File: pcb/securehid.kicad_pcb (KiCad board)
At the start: 2 copper layers, 129 x 69 mm, 193 parts, among them J1 USB_B_Micro, J2 SWD_HOST, J3 UART_HOST, J4 SWD_DEVICE, J5 UART_DEVICE, J6 USB_A, J7 USB_SPARE, J8 USB_A, Q1 AO3400, Q2 AO3400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

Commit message: Some cleanups
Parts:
- removed the REF** at (65.2, 63.0)
- removed the REF** at (65.2, 99.0)
- added REF**: MountingHole_2.7mm_M2.5, MountingHole:MountingHole_2.7mm_M2.5, F.Cu at (96.5, 108.5)
- added REF**: MountingHole_2.7mm_M2.5, MountingHole:MountingHole_2.7mm_M2.5, F.Cu at (146.5, 108.5)
- added REF**: MountingHole_2.7mm_M2.5, MountingHole:MountingHole_2.7mm_M2.5, F.Cu at (146.5, 53.5)
- added REF**: MountingHole_2.7mm_M2.5, MountingHole:MountingHole_2.7mm_M2.5, F.Cu at (96.5, 53.5)
- added REF**: MountingHole_2.7mm_M2.5, MountingHole:MountingHole_2.7mm_M2.5, F.Cu at (51.5, 53.5)
- added REF**: MountingHole_2.7mm_M2.5, MountingHole:MountingHole_2.7mm_M2.5, F.Cu at (51.5, 108.5)
- added TP81: TestPoint_Alt, TestPoint:TestPoint_Pad_1.0x1.0mm, B.Cu at (115.0, 82.2)
- added TP82: TestPoint_Alt, TestPoint:TestPoint_Pad_1.0x1.0mm, B.Cu at (115.0, 85.8)
- added TP83: TestPoint_Alt, TestPoint:TestPoint_Pad_1.0x1.0mm, B.Cu at (115.0, 84.0)
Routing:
- net GND: track 91.3 -> 98.1 mm, vias 9 -> 39
- net /SECURE_IF_F4RX: track 49.8 -> 51.8 mm, vias 0 -> 1
- net /SECURE_IF_F4TX: track 51.1 -> 52.8 mm, vias 0 -> 1
- net GNDA: vias 2 -> 38
- net (no net): vias 0 -> 1
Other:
- outline, holes or cut-outs redrawn

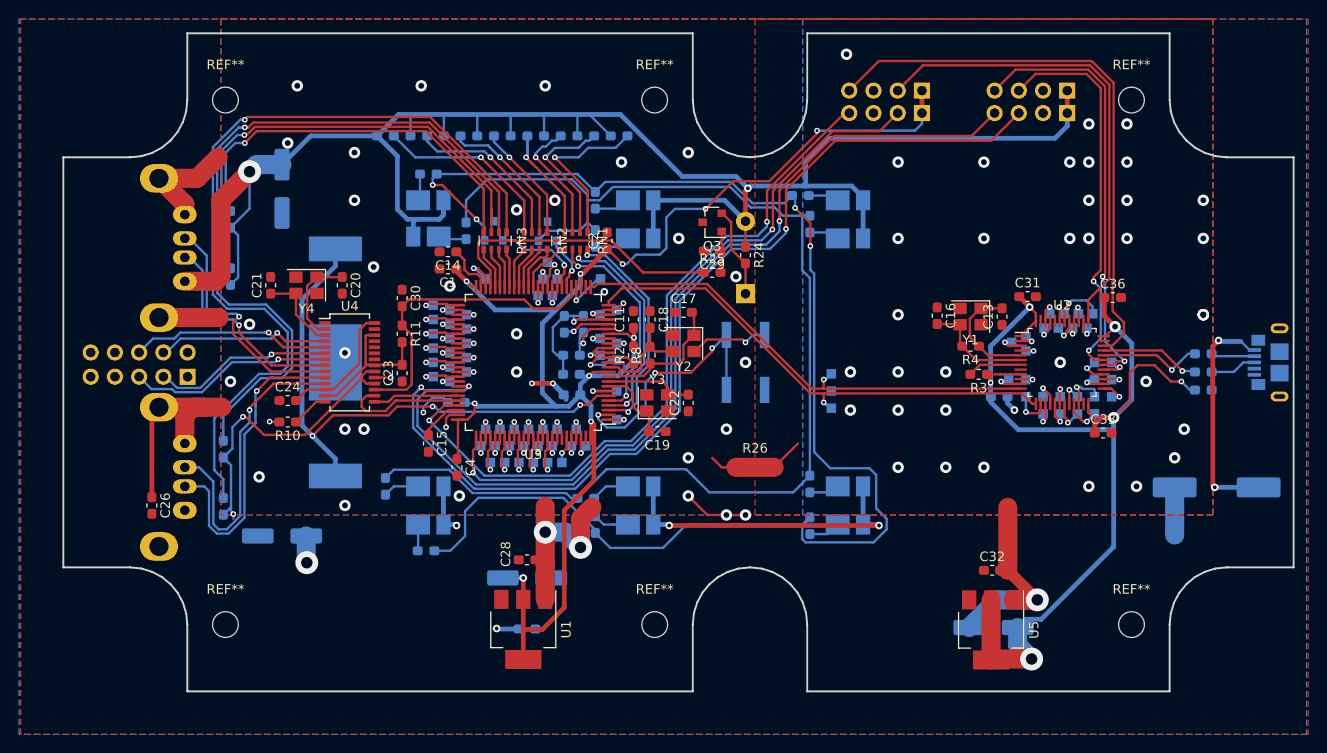
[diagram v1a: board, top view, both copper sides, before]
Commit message: Further PCB cleanup, initial silk cleanup
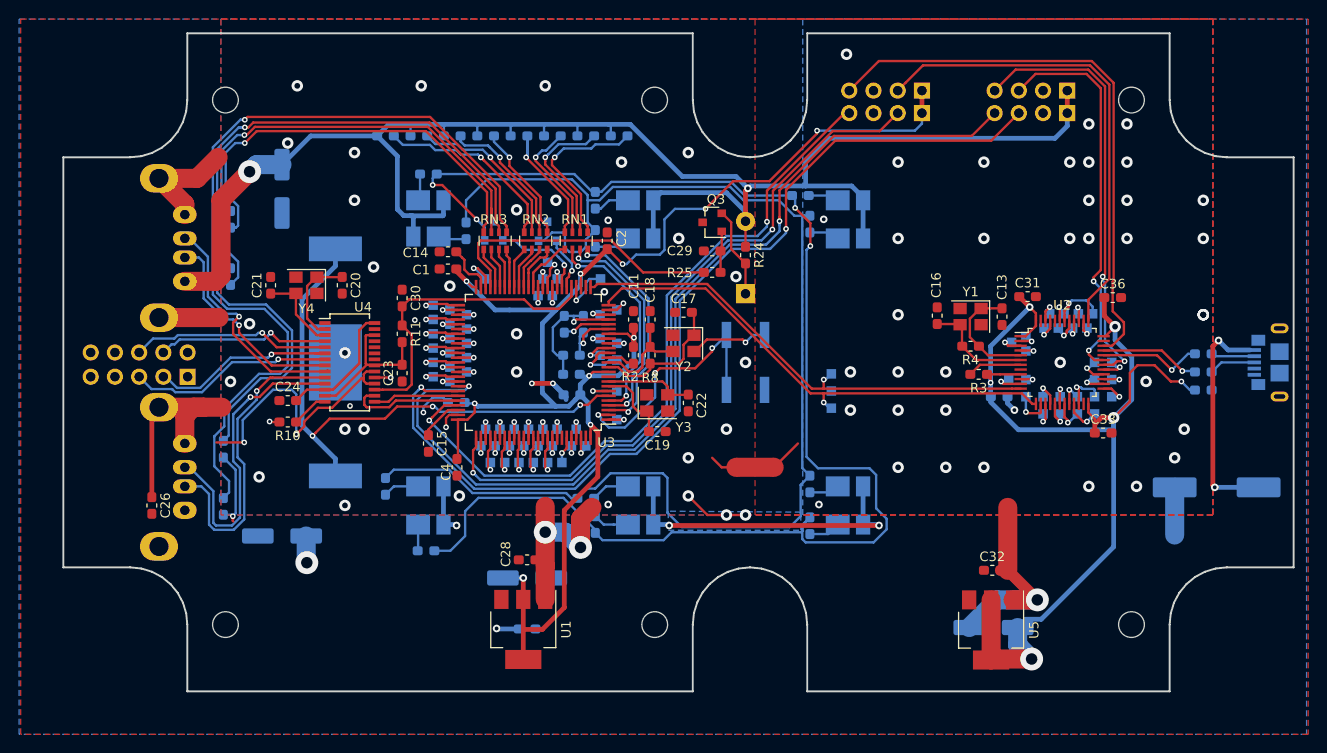
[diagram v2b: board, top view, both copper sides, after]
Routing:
- net VBUS: track 315.6 -> 295.0 mm, vias 11 -> 12
- net Net-(Q1-Pad2): track 128.7 -> 138.8 mm
- net /USBH_DP: track 13.0 -> 12.1 mm
- net Net-(J8-Pad3): track 25.9 -> 25.2 mm
- net GNDA: vias 38 -> 40
- net GND: vias 39 -> 43
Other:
- board text added: "M2.5"
